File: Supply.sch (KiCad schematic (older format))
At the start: 20 parts, among them IC6 JW5052C, IC7 JW5052C, IC8 B1212S-2W

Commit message: first commit of Amalga_100.
R2D needs to be finished.
Logicpart needs to be routed.
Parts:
- removed C41, C42, C45, C46: 22u, Capacitor_SMD:C_0805_2012Metric, symbol Device:C
- removed C43, C44: 100n, Capacitor_SMD:C_0805_2012Metric, symbol Device:C_Small
- removed C47, C48: 2u2, Capacitor_SMD:C_0805_2012Metric, symbol Device:C_Small
- removed IC6, IC7: JW5052C, Package_TO_SOT_SMD:TSOT-23-6, symbol HSWR-V2-rescue:JW5052C-Auktoralib
- removed IC8: B1212S-2W, Converter_DCDC:Converter_DCDC_muRata_NMAxxxxSC_THT, symbol HSWR-V2-rescue:DCDC_6pin-Auktoralib
- removed L1, L2: FCI201209F-4R7K, Inductor_SMD:L_0805_2012Metric, symbol Device:L
- removed NT1: Net-Tie_2, NetTie:NetTie-2_SMD_Pad2.0mm, symbol Device:Net-Tie_2
- removed R44, R45: 100k, Resistor_SMD:R_0805_2012Metric, symbol Device:R_Small
- removed R46: 110k, Resistor_SMD:R_0805_2012Metric, symbol Device:R_Small
- removed R47: 15k, Resistor_SMD:R_0805_2012Metric, symbol Device:R_Small
- removed R48: 49k9, Resistor_SMD:R_0805_2012Metric, symbol Device:R_Small
- removed R49: 11k, Resistor_SMD:R_0805_2012Metric, symbol Device:R_Small
- added C27, C4, C5, C8: 22u, Capacitor_SMD:C_0805_2012Metric, symbol Amalga_100-rescue:C-Device
- added C3, C47: 2u2, Capacitor_SMD:C_0805_2012Metric, symbol Amalga_100-rescue:C-Device
- added C6, C7: 100n, Capacitor_SMD:C_0805_2012Metric, symbol Amalga_100-rescue:C-Device
- added L1, L2: 4.7uH, Inductors_SMD:L_Wuerth_MAPI-3020, symbol Amalga_100-rescue:INDUCTOR-HSWR-V2-rescue
- added R39: 28k, Resistor_SMD:R_0805_2012Metric, symbol Amalga_100-rescue:R-Device
- added R40: 100k, Resistor_SMD:R_0805_2012Metric, symbol Amalga_100-rescue:R-Device
- added R41: 110k, Resistor_SMD:R_0805_2012Metric, symbol Amalga_100-rescue:R-Device
- added R42: 15k, Resistor_SMD:R_0805_2012Metric, symbol Amalga_100-rescue:R-Device
- added R43: 49k9, Resistor_SMD:R_0805_2012Metric, symbol Amalga_100-rescue:R-Device
- added R44: 11k, Resistor_SMD:R_0805_2012Metric, symbol Amalga_100-rescue:R-Device
- added U2: B1215S-2W, Converters_DCDC_ACDC:DCDC-Conv_TRACO_TMR_1-xxxx_Single, symbol Amalga_100-rescue:B1215S-2W-B1215s-2w
- added U3, U4: JW5052C, Package_TO_SOT_SMD:SOT-23-6, symbol Amalga_100-rescue:JW5052C-JW5052c
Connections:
- net labels added: +15V
- net labels removed: +12V, GNDPWR
- wire segments 11 -> 62

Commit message: continued Resolver continued Routing
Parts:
- U2: footprint Converters_DCDC_ACDC:DCDC-Conv_TRACO_TMR_1-xxxx_Single -> Converter_DCDC:Converter_DCDC_TRACO_TMR-1-xxxx_Single_THT
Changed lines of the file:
@@
 F 0 "U2" H 3350 3067 50  0000 C CNN
 F 1 "B1215S-2W" H 3350 2976 50  0000 C CNN
-F 2 "Converters_DCDC_ACDC:DCDC-Conv_TRACO_TMR_1-xxxx_Single" H 3300 3000 50  0001 C CNN
+F 2 "Converter_DCDC:Converter_DCDC_TRACO_TMR-1-xxxx_Single_THT" H 3300 3000 50  0001 C CNN
 F 3 "" H 3300 3000 50  0001 C CNN
 	1    3300 2600

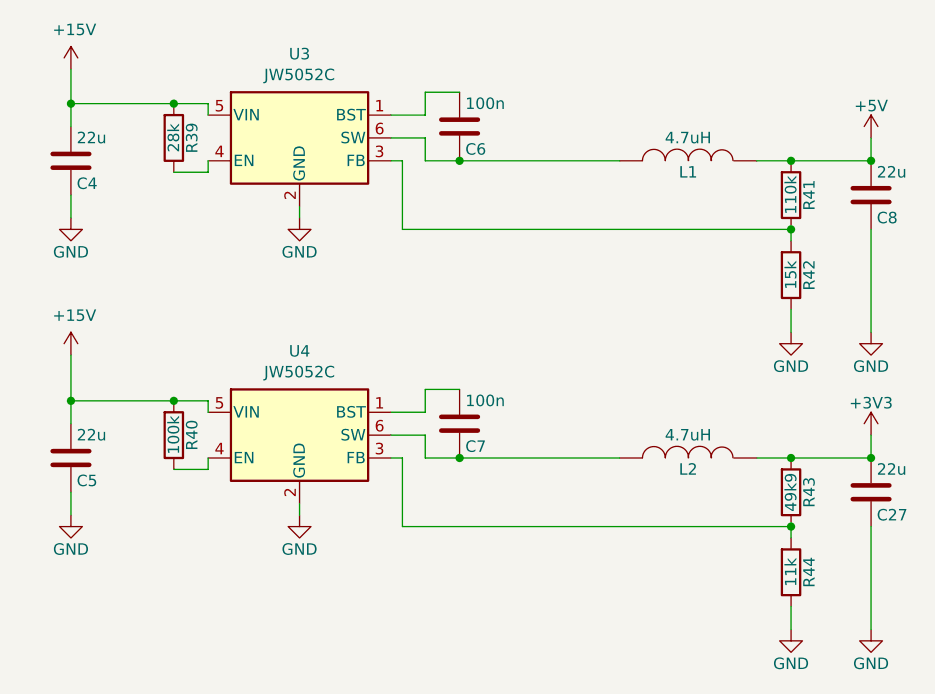
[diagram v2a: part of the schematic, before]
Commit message: -changed supply ics:  B1215S-2W to SPU02M-15  JW5052C to XRP7659
-added schottky-diode needed by XRP7659

-updated BOM
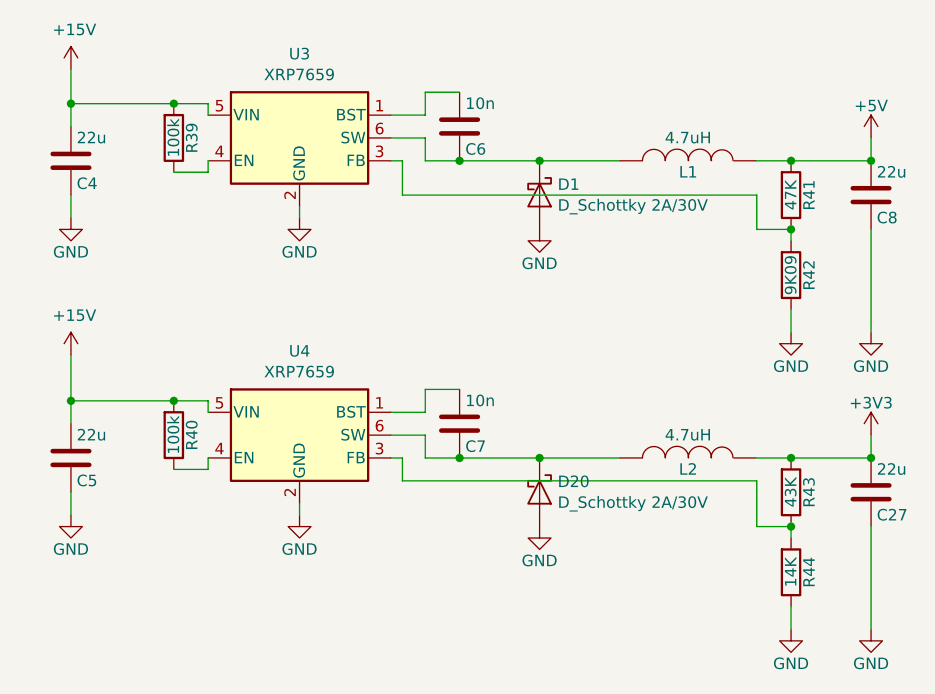
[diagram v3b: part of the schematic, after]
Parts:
- added D1, D20: D_Schottky 2A/30V, symbol device:D_Schottky
- C6, C7: value 100n -> 10n
- R39: value 28k -> 100k
- R41: value 110k -> 47K
- R42: value 15k -> 9K09
- R43: value 49k9 -> 43K
- R44: value 11k -> 14K
- U3, U4: value JW5052C -> XRP7659
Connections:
- net GND: now also D1.2 (A), D20.2 (A)
- net at C6.1, L1.2, U3.6 (SW): now also D1.1 (K)
- net at C7.1, L2.2, U4.6 (SW): now also D20.1 (K)
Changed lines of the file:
@@
 EESchema Schematic File Version 4
 LIBS:Amalga_100-cache
-EELAYER 26 0
+EELAYER 29 0
 EELAYER END
 $Descr A4 11693 8268
@@
 P 6000 2350
 F 0 "U3" H 6000 2717 50  0000 C CNN
-F 1 "JW5052C" H 6000 2626 50  0000 C CNN
+F 1 "XRP7659" H 6000 2626 50  0000 C CNN
 F 2 "Package_TO_SOT_SMD:SOT-23-6" H 6050 2100 50  0001 L CNN
 F 3 "http://www.ti.com/lit/ds/symlink/tps563200.pdf" H 6000 2350 50  0001 C CNN
@@
 P 5450 2350
 F 0 "R39" V 5530 2350 50  0000 C CNN
-F 1 "28k" V 5450 2350 50  0000 C CNN
+F 1 "100k" V 5450 2350 50  0000 C CNN
 F 2 "Resistor_SMD:R_0805_2012Metric" V 5380 2350 50  0001 C CNN
 F 3 "" H 5450 2350 50  0000 C CNN
@@
 P 8150 2600
 F 0 "R41" V 8230 2600 50  0000 C CNN
-F 1 "110k" V 8150 2600 50  0000 C CNN
+F 1 "47K" V 8150 2600 50  0000 C CNN
 F 2 "Resistor_SMD:R_0805_2012Metric" V 8080 2600 50  0001 C CNN
 F 3 "" H 8150 2600 50  0000 C CNN
@@
 P 8150 2950
 F 0 "R42" V 8230 2950 50  0000 C CNN
-F 1 "15k" V 8150 2950 50  0000 C CNN
+F 1 "9K09" V 8150 2950 50  0000 C CNN
 F 2 "Resistor_SMD:R_0805_2012Metric" V 8080 2950 50  0001 C CNN
 F 3 "" H 8150 2950 50  0000 C CNN
@@
 AR Path="/5899E25F/5CA7636C" Ref="C6"  Part="1"
 F 0 "C6" H 6725 2400 50  0000 L CNN
-F 1 "100n" H 6725 2200 50  0000 L CNN
+F 1 "10n" H 6725 2200 50  0000 L CNN
 F 2 "Capacitor_SMD:C_0805_2012Metric" H 6738 2150 50  0001 C CNN
 F 3 "" H 6700 2300 50  0000 C CNN
@@
 Wire Wire Line
 	6400 2450 6450 2450
-Wire Wire Line
-	6450 2450 6450 2750
-Wire Wire Line
-	6450 2750 8150 2750
 $Comp
 L Amalga_100-rescue:C-Device C?
@@
 	0    1    -1   0
 $EndComp
-Connection ~ 8150 2750
 Wire Wire Line
 	8150 2450 8000 2450
 Connection ~ 6700 2450
-Wire Wire Line
-	6700 2450 7400 2450
 Wire Wire Line
 	8500 2450 8150 2450
@@
 P 6000 3650
 F 0 "U4" H 6000 4017 50  0000 C CNN
-F 1 "JW5052C" H 6000 3926 50  0000 C CNN
+F 1 "XRP7659" H 6000 3926 50  0000 C CNN
 F 2 "Package_TO_SOT_SMD:SOT-23-6" H 6050 3400 50  0001 L CNN
 F 3 "http://www.ti.com/lit/ds/symlink/tps563200.pdf" H 6000 3650 50  0001 C CNN
@@
 P 8150 3900
 F 0 "R43" V 8230 3900 50  0000 C CNN
-F 1 "49k9" V 8150 3900 50  0000 C CNN
+F 1 "43K" V 8150 3900 50  0000 C CNN
 F 2 "Resistor_SMD:R_0805_2012Metric" V 8080 3900 50  0001 C CNN
 F 3 "" H 8150 3900 50  0000 C CNN
@@
 P 8150 4250
 F 0 "R44" V 8230 4250 50  0000 C CNN
-F 1 "11k" V 8150 4250 50  0000 C CNN
+F 1 "14K" V 8150 4250 50  0000 C CNN
 F 2 "Resistor_SMD:R_0805_2012Metric" V 8080 4250 50  0001 C CNN
 F 3 "" H 8150 4250 50  0000 C CNN
@@
 AR Path="/5899E25F/5CAA83A8" Ref="C7"  Part="1"
 F 0 "C7" H 6725 3700 50  0000 L CNN
-F 1 "100n" H 6725 3500 50  0000 L CNN
+F 1 "10n" H 6725 3500 50  0000 L CNN
 F 2 "Capacitor_SMD:C_0805_2012Metric" H 6738 3450 50  0001 C CNN
 F 3 "" H 6700 3600 50  0000 C CNN
@@
 Wire Wire Line
 	6400 3750 6450 3750
-Wire Wire Line
-	6450 3750 6450 4050
-Wire Wire Line
-	6450 4050 8150 4050
 $Comp
 L Amalga_100-rescue:C-Device C?
@@
 	0    1    -1   0
 $EndComp
-Connection ~ 8150 4050
 Wire Wire Line
 	8150 3750 8000 3750
 Connection ~ 6700 3750
 Wire Wire Line
-	6700 3750 7400 3750
+	6700 3750 7050 3750
 Wire Wire Line
 	8500 3750 8150 3750
@@
 	1    0    0    -1
 $EndComp
+Wire Wire Line
+	6700 2450 7050 2450
+Wire Wire Line
+	6450 2450 6450 2600
+Wire Wire Line
+	6450 2600 8000 2600
+Wire Wire Line
+	8000 2600 8000 2750
+Wire Wire Line
+	8000 2750 8150 2750
+Connection ~ 8150 2750
+Wire Wire Line
+	8150 4050 8000 4050
+Wire Wire Line
+	8000 4050 8000 3850
+Wire Wire Line
+	8000 3850 6450 3850
+Wire Wire Line
+	6450 3850 6450 3750
+Connection ~ 8150 4050
+$Comp
+L device:D_Schottky D1
+U 1 1 5CCFBB96
+P 7050 2600
+F 0 "D1" V 7004 2679 50  0000 L CNN
+F 1 "D_Schottky 2A/30V" V 7095 2679 50  0000 L CNN
+F 2 "" H 7050 2600 50  0001 C CNN
+F 3 "~" H 7050 2600 50  0001 C CNN
+	1    7050 2600
+	0    1    1    0
+$EndComp
+Connection ~ 7050 2450
+Wire Wire Line
+	7050 2450 7400 2450
+$Comp
+L device:D_Schottky D20
+U 1 1 5CCFC5EB
+P 7050 3900
+F 0 "D20" V 7004 3979 50  0000 L CNN
+F 1 "D_Schottky 2A/30V" V 7095 3979 50  0000 L CNN
+F 2 "" H 7050 3900 50  0001 C CNN
+F 3 "~" H 7050 3900 50  0001 C CNN
+	1    7050 3900
+	0    1    1    0
+$EndComp
+Connection ~ 7050 3750
+Wire Wire Line
+	7050 3750 7400 3750
+$Comp
+L Amalga_100-rescue:GND-power #PWR060
+U 1 1 5CCFCF3F
+P 7050 4050
+F 0 "#PWR060" H 7050 3800 50  0001 C CNN
+F 1 "GND" H 7050 3900 50  0000 C CNN
+F 2 "" H 7050 4050 60  0000 C CNN
+F 3 "" H 7050 4050 60  0000 C CNN
+	1    7050 4050
+	1    0    0    -1
+$EndComp
+$Comp
+L Amalga_100-rescue:GND-power #PWR059
+U 1 1 5CCFF616
+P 7050 2750
+F 0 "#PWR059" H 7050 2500 50  0001 C CNN
+F 1 "GND" H 7050 2600 50  0000 C CNN
+F 2 "" H 7050 2750 60  0000 C CNN
+F 3 "" H 7050 2750 60  0000 C CNN
+	1    7050 2750
+	1    0    0    -1
+$EndComp
